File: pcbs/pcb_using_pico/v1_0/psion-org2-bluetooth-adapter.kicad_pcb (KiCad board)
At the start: 2 copper layers, 129.7 x 100 mm, 48 parts, among them J1 Conn_02x08_Odd_Even, J2 Conn_01x03_Female, J3 Barrel_Jack, J4 Connector_USB_B_Micro, J5 Conn_01x04_Female, J7 Conn_01x03_Female, M1 P-CHANNEL-MOSFET, U1 74LS245, U2 74LS245, U3 Pico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

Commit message: Merged erroneous changes to V1.0 archive started
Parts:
- added R7: R_Small, Resistor_SMD:R_0805_2012Metric, F.Cu at (160.8, 115.5)
- added R8: R_Small, Resistor_SMD:R_0805_2012Metric, F.Cu at (160.8, 112.6)
- moved J5 9.28 mm to (121.4, 136.9), turned to 180 degrees
- moved R4 9.22 mm to (116.5, 136.9)
- moved JP3 8.32 mm to (111.7, 128.1)
- moved JP2 4.86 mm to (128.1, 132.6)
- moved JP4 4.80 mm to (128.1, 135.4)
- moved R5 4.17 mm to (116.5, 134.3)
- moved JP1 4.12 mm to (111.7, 130.8)
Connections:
- J4 pad 5: (no net) -> GND
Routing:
- net GND: track 613.8 -> 653.0 mm, vias 20 -> 21
- net Net-(R7-Pad2): track 0.00 -> 26.1 mm
- net Net-(J5-Pad4): track 6.68 -> 11.1 mm
- net Net-(J5-Pad3): track 8.43 -> 12.2 mm
- net +3V3: track 157.2 -> 161.0 mm, vias 10 -> 11
- net VREG: track 134.8 -> 137.5 mm, vias 4 -> 5
- net I2C_SDA: track 79.8 -> 78.5 mm, vias 4 -> 2
- net I2C_SCLK: track 43.1 -> 44.4 mm, vias 2 -> 3
- added copper zone on F.Cu, net GND

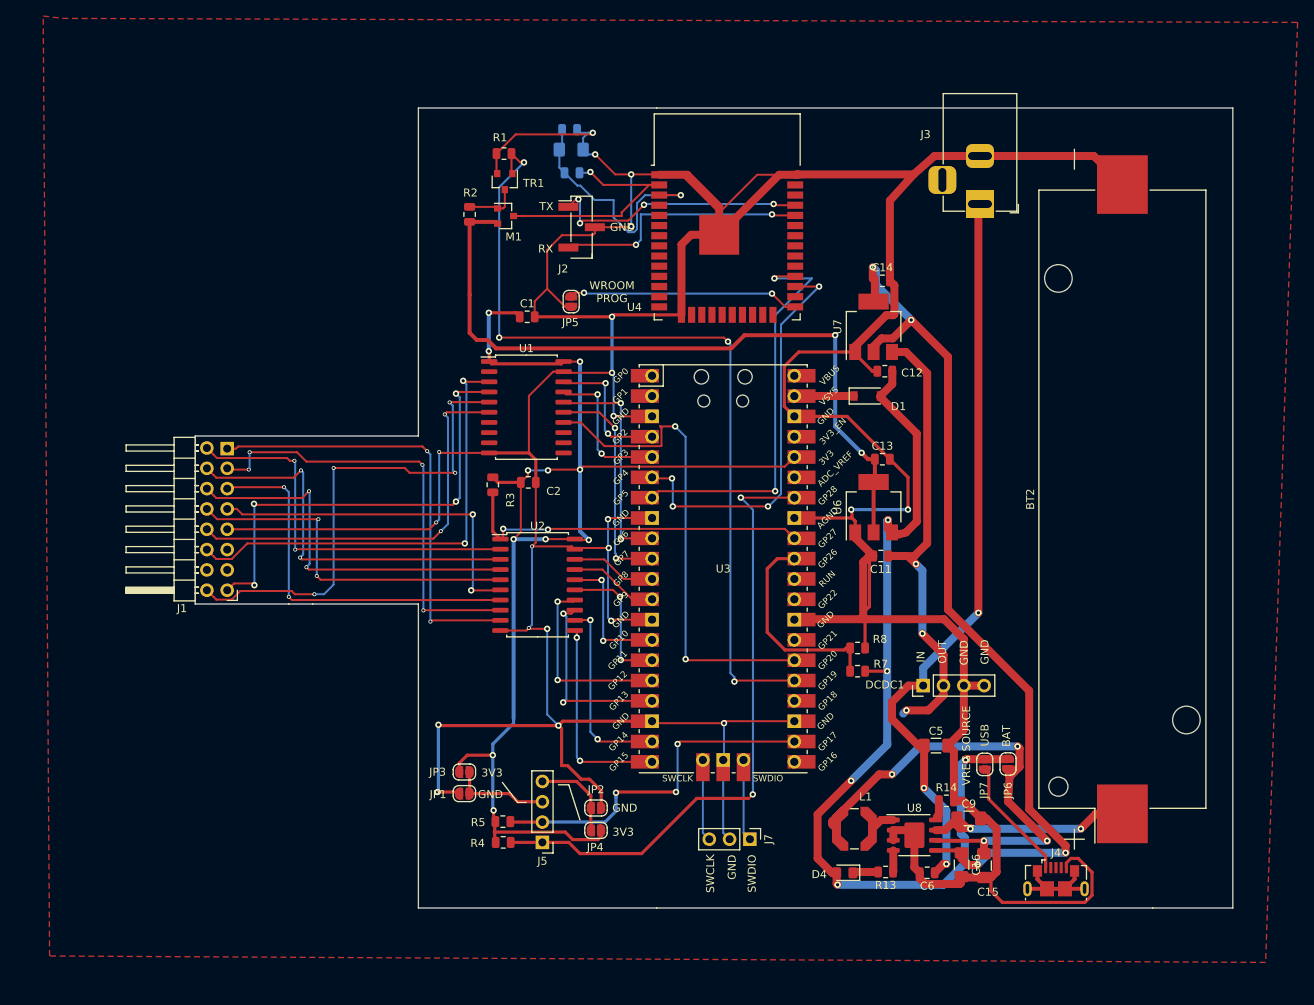
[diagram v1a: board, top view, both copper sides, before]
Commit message: V2.0 sent off for fab. New charger IC with more solderable footprint, plus other fixes
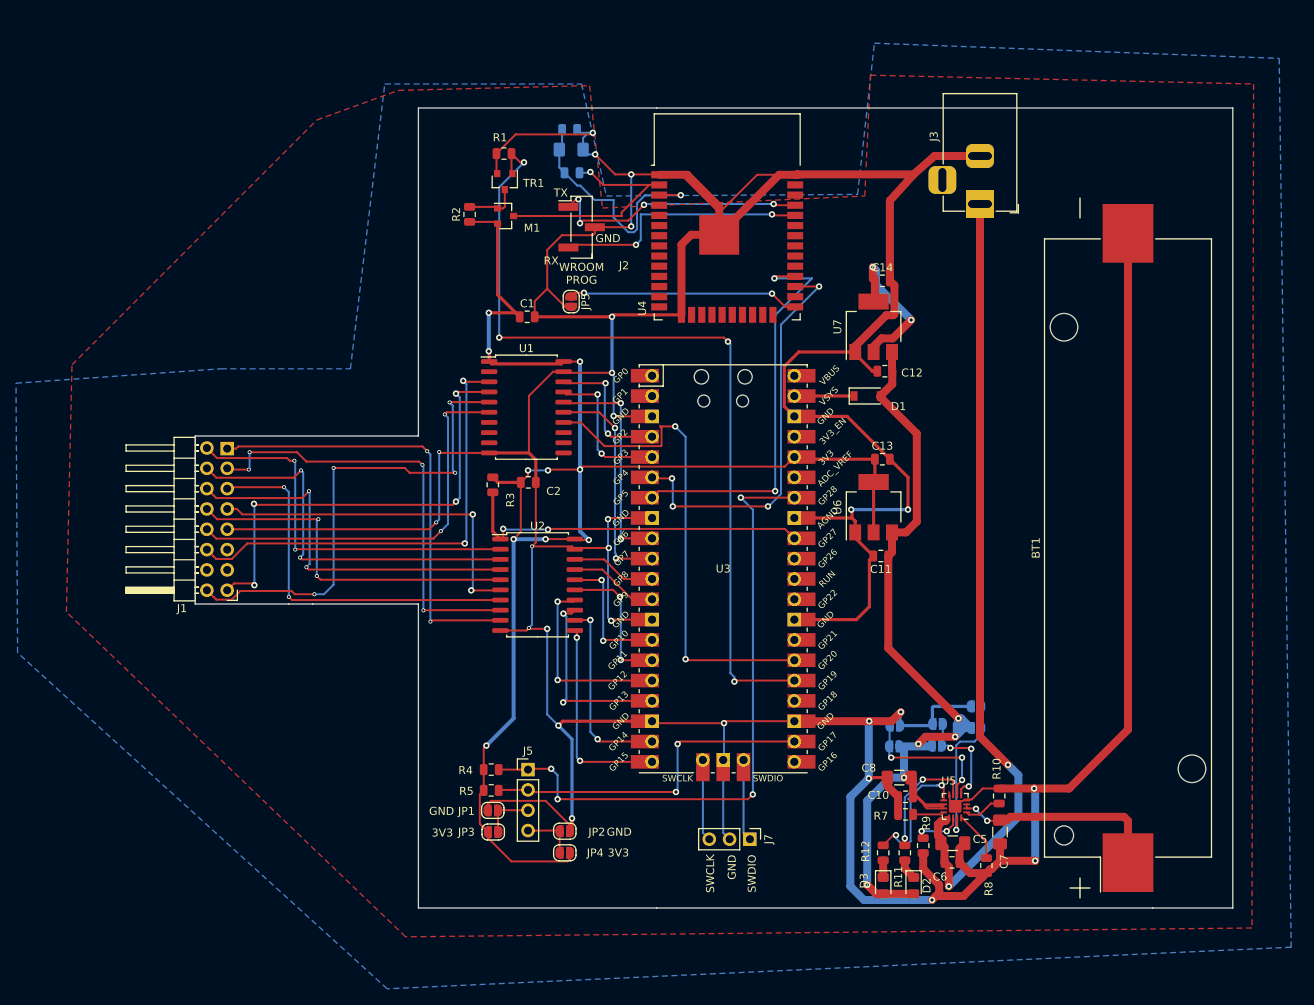
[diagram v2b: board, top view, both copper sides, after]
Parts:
- removed BT2: Battery_Cell, Battery:BatteryHolder_Keystone_1042_1x18650
- removed C15: 22uF, Capacitor_SMD:C_1206_3216Metric_Pad1.42x1.75mm_HandSolder
- removed C16: 10uF, Capacitor_SMD:C_1206_3216Metric_Pad1.42x1.75mm_HandSolder
- removed C9: 1uF, Capacitor_SMD:C_1206_3216Metric_Pad1.42x1.75mm_HandSolder
- removed D4: LED, LED_SMD:LED_0805_2012Metric_Pad1.15x1.40mm_HandSolder
- removed DCDC1: dcdc, Connector_PinHeader_2.54mm:PinHeader_1x04_P2.54mm_Vertical
- removed J4: Connector_USB_B_Micro, Connector_USB:USB_Micro-B_GCT_USB3076-30-A
- removed L1: 2.2uH, Inductor_SMD:L_Coilcraft_LPS5030
- removed R13: 2k2, Resistor_SMD:R_0805_2012Metric
- removed R14: 500R, Resistor_SMD:R_0805_2012Metric
- removed U8: ETA6002, Package_SO:SOIC-8-1EP_3.9x4.9mm_P1.27mm_EP2.514x3.2mm
- added BT1: Battery_Cell, Battery:BatteryHolder_Keystone_1042_1x18650, F.Cu at (194.6, 100.1)
- added C10: 100nF, Capacitor_SMD:C_0805_2012Metric, F.Cu at (166.8, 131.2)
- added C7: 4u7, Capacitor_SMD:C_1206_3216Metric_Pad1.42x1.75mm_HandSolder, F.Cu at (178.6, 135.6)
- added C8: 10uF, Capacitor_SMD:C_1206_3216Metric_Pad1.42x1.75mm_HandSolder, F.Cu at (166.0, 128.8)
- added D2: LED, LED_SMD:LED_0805_2012Metric_Pad1.15x1.40mm_HandSolder, F.Cu at (167.8, 142.3)
- added D3: LED, LED_SMD:LED_0805_2012Metric_Pad1.15x1.40mm_HandSolder, F.Cu at (164.0, 142.3)
- added JP10: Jumper_NO_Small, Jumper:SolderJumper-2_P1.3mm_Open_RoundedPad1.0x1.5mm, B.Cu at (175.6, 122.6)
- added JP11: Jumper_NO_Small, Jumper:SolderJumper-2_P1.3mm_Open_RoundedPad1.0x1.5mm, B.Cu at (175.6, 119.9)
- added JP8: Jumper_NO_Small, Jumper:SolderJumper-2_P1.3mm_Open_RoundedPad1.0x1.5mm, B.Cu at (170.7, 124.8)
- added JP9: Jumper_NO_Small, Jumper:SolderJumper-2_P1.3mm_Open_RoundedPad1.0x1.5mm, B.Cu at (170.8, 122.1)
- added R10: 10k, Resistor_SMD:R_0805_2012Metric, F.Cu at (178.5, 131.1)
- added R11: R_Small, Resistor_SMD:R_0805_2012Metric, F.Cu at (166.7, 138.2)
- added R12: R_Small, Resistor_SMD:R_0805_2012Metric, F.Cu at (164.0, 138.2)
- added R9: R_Small, Resistor_SMD:R_0805_2012Metric, F.Cu at (169.0, 137.3)
- added U5: BQ24072RGT, Package_DFN_QFN:VQFN-16-1EP_3x3mm_P0.5mm_EP1.6x1.6mm, F.Cu at (173.0, 132.4)
- JP6, JP7: moved to B.Cu
- moved R8 31.6 mm to (176.9, 139.8), turned to 270 degrees
- moved R7 18.9 mm to (166.8, 133.4)
- moved JP6 14.4 mm to (165.4, 124.9), turned to 180 degrees
- moved C5 12.4 mm to (172.7, 137.0)
- moved JP7 12.3 mm to (165.4, 122.3), turned to 180 degrees
- moved J5 9.28 mm to (119.6, 127.8), turned to 0 degrees
- moved R4 9.22 mm to (115.0, 127.8)
- moved JP3 8.32 mm to (115.2, 135.6)
- moved JP2 4.86 mm to (124.2, 135.5)
- moved JP4 4.80 mm to (124.2, 138.2)
- moved R5 4.17 mm to (115.0, 130.4)
- moved JP1 4.12 mm to (115.2, 132.9)
- moved C6 3.36 mm to (172.6, 139.4), turned to 0 degrees
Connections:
- net Net-(C14-Pad1) renamed +5V
- net Net-(C5-Pad1) renamed VIN
- C11 pad 1: Net-(C11-Pad1) -> VREG
- C13 pad 1: ESP_3V3 -> +3V3
- JP6 pad 2: Net-(C15-Pad1) -> Net-(JP6-Pad2)
- JP7 pad 1: VREG -> GND
- JP7 pad 2: Net-(J4-Pad1) -> Net-(JP6-Pad2)
- M1 pad 2: ESP_3V3 -> +3V3
- R2 pad 1: ESP_3V3 -> +3V3
- R7 pad 1: VREG -> Net-(R7-Pad1)
- R7 pad 2: Net-(R7-Pad2) -> GND
- R8 pad 1: Net-(R7-Pad2) -> Net-(R8-Pad1)
- U3 pad 31: Net-(R7-Pad2) -> Net-(U3-Pad31)
- U6 pad 2: ESP_3V3 -> +3V3
- U7 pad 3: Net-(C11-Pad1) -> VREG
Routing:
- net +5V: track 112.5 -> 19.8 mm, vias 4 -> 2
- net ESP_3V3: track 91.9 -> 0.00 mm, vias 2 -> 0
- net Net-(C15-Pad1): track 59.2 -> 0.00 mm, vias 4 -> 0
- net Net-(C11-Pad1): track 57.3 -> 0.00 mm, vias 3 -> 0
- net GND: track 653.0 -> 699.0 mm, vias 21 -> 26
- net Net-(BT2-Pad1): track 28.0 -> 0.00 mm, vias 2 -> 0
- net +3V3: track 161.0 -> 188.7 mm, vias 11 -> 10
- net Net-(BT1-Pad1): track 0.00 -> 27.0 mm, vias 0 -> 2
- net Net-(R7-Pad2): track 26.1 -> 0.00 mm
- net VREG: track 137.5 -> 114.1 mm
- net Net-(JP10-Pad1): track 0.00 -> 19.3 mm, vias 0 -> 1
- net Net-(JP6-Pad2): track 0.00 -> 17.9 mm, vias 0 -> 3
- net Net-(R12-Pad2): track 0.00 -> 17.0 mm, vias 0 -> 2
- net Net-(J4-Pad1): track 15.4 -> 0.00 mm
- net Net-(R11-Pad2): track 0.00 -> 14.8 mm, vias 0 -> 2
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- added copper zone on B.Cu, net +3V3
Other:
- board text added: "EN1"
- board text added: "EN2"
- board text added: "Psion Organiser II Bluetooth Adapter Dec 2021 menadue@gmail.com V1.0"
- board text added: "TD"
- board text added: "VREG"
- board text removed: "BAT"
- board text removed: "IN"
- board text removed: "OUT"
- board text removed: "Psion Organiser II Bluetooth Adapter Feb 2022 menadue@gmail.com V2.0"
- board text removed: "USB"
- board text removed: "VREG SOURCE"
